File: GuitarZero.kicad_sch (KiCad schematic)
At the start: 17 parts, among them J1 USB_A, J2 USB_B_Micro, J3 AudioJack3_SwitchT, SW1 SW_Push, SW2 SW_Push, SW3 SW_Push, SW4 SW_Push, SW5 SW_Push, SW6 SW_Push

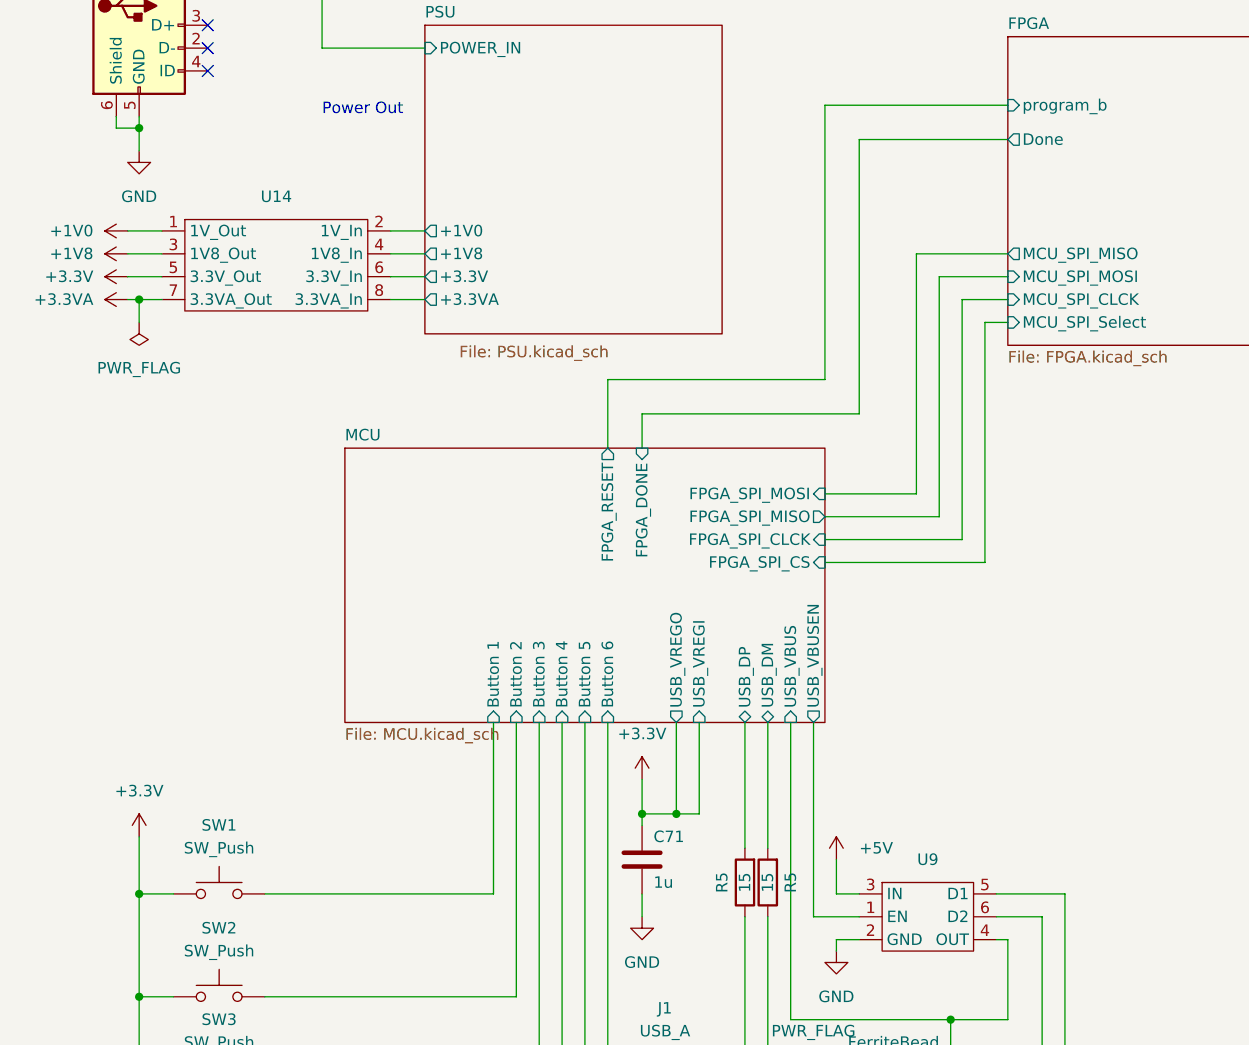
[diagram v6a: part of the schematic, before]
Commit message: Added footprints to symbols
Some nice light work
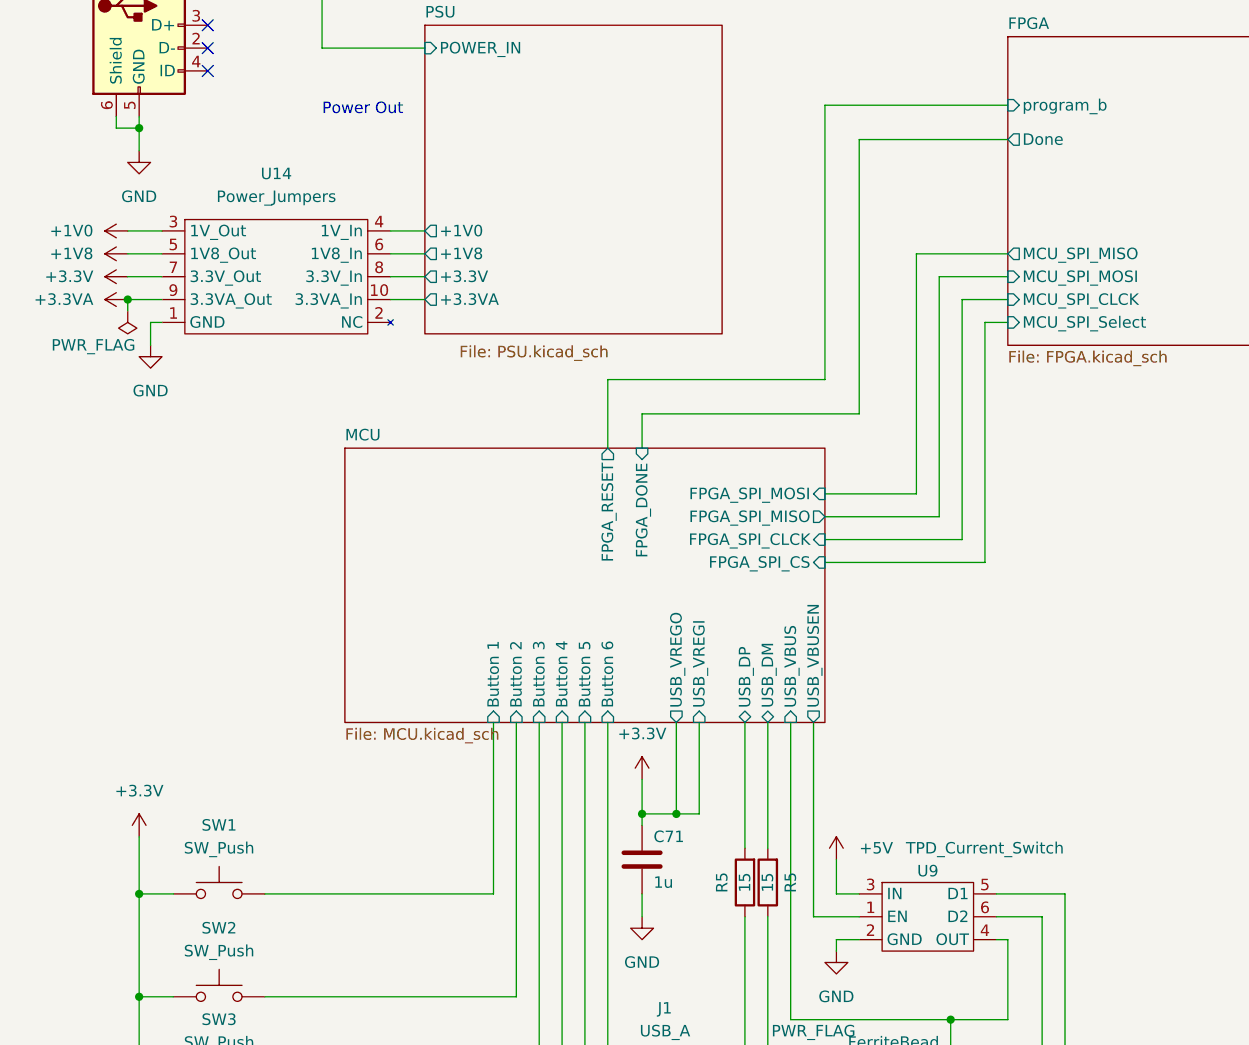
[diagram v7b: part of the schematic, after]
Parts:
- C71, C9: footprint (none) -> Capacitor_SMD:C_1206_3216Metric
- FB1: footprint (none) -> Inductor_SMD:L_0603_1608Metric
- J1: footprint (none) -> Connector_USB:USB_A_Stewart_SS-52100-001_Horizontal
- J2: footprint (none) -> Connector_USB:USB_Micro-B_Amphenol_10103594-0001LF_Horizontal
- J3: footprint (none) -> Connector_Audio:Jack_3.5mm_CUI_SJ-3524-SMT_Horizontal
- LS1: footprint (none) -> Resistor_SMD:R_2010_5025Metric
- R5: footprint (none) -> Resistor_SMD:R_1206_3216Metric
- SW1, SW2, SW3, SW4, SW5, SW6: footprint (none) -> Button_Switch_THT:SW_CW_GPTS203211B
- U14: value ~ -> Power_Jumpers; footprint (none) -> Connector_PinHeader_2.54mm:PinHeader_2x05_P2.54mm_Vertical
- U9: value ~ -> TPD_Current_Switch; footprint (none) -> TPD3S:SOT95P280X145-6N
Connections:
- net +1V0: now also U14.3 (1V_Out); no longer U14.1 (1V_Out)
- net +1V8: now also U14.5 (1V8_Out); no longer U14.3 (1V8_Out)
- net +3.3V: now also U14.7 (3.3V_Out); no longer U14.5 (3.3V_Out)
- net +3.3VA: now also U14.9 (3.3VA_Out); no longer U14.7 (3.3VA_Out)
- net GND: now also U14.1 (GND)
- net PSU/+1V0: now also U14.4 (1V_In); no longer U14.2 (1V_In)
- net PSU/+1V8: now also U14.6 (1V8_In); no longer U14.4 (1V8_In)
- net PSU/+3.3V: now also U14.8 (3.3V_In); no longer U14.6 (3.3V_In)
- net PSU/+3.3VA: now also U14.10 (3.3VA_In); no longer U14.8 (3.3VA_In)

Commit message: Changed Reistor and Capacitor size fomr 1206 to 0805
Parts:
- C71, C9: footprint Capacitor_SMD:C_1206_3216Metric -> Capacitor_SMD:C_0805_2012Metric
- R5: footprint Resistor_SMD:R_1206_3216Metric -> Resistor_SMD:R_0805_2012Metric
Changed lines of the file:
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@@
       (effects (font (size 1.27 1.27)))
     )
-    (property "Footprint" "Resistor_SMD:R_1206_3216Metric" (at 93.218 119.38 90)
+    (property "Footprint" "Resistor_SMD:R_0805_2012Metric" (at 93.218 119.38 90)
       (effects (font (size 1.27 1.27)) hide)
     )
@@
       (effects (font (size 1.27 1.27)))
     )
-    (property "Footprint" "Resistor_SMD:R_1206_3216Metric" (at 95.758 119.38 90)
+    (property "Footprint" "Resistor_SMD:R_0805_2012Metric" (at 95.758 119.38 90)
       (effects (font (size 1.27 1.27)) hide)
     )
@@
       (effects (font (size 1.27 1.27)) (justify left))
     )
-    (property "Footprint" "Capacitor_SMD:C_1206_3216Metric" (at 80.9752 120.65 0)
+    (property "Footprint" "Capacitor_SMD:C_0805_2012Metric" (at 80.9752 120.65 0)
       (effects (font (size 1.27 1.27)) hide)
     )
@@
       (effects (font (size 1.27 1.27)) (justify left))
     )
-    (property "Footprint" "Capacitor_SMD:C_1206_3216Metric" (at 100.0252 157.48 0)
-      (effects (font (size 1.27 1.27)) hide)
-    )
+    (property "Footprint" "Capacitor_SMD:C_0805_2012Metric" (at 100.0252 157.48 0)
+      (effects (font (size 1.27 1.27)) hide)
+    )
